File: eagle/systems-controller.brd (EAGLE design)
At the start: 80 x 40 mm, 52 parts, among them IC1 MK20DX256VLH7, IC2 MKL02Z32VFG4, IC3 TPS6214XRGT, J1 SIG, J2 PWR, J3 GND, Q1 FA-238, Q2 PMV20ENR, Q3 PMV20ENR, Q4 PMV20ENR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

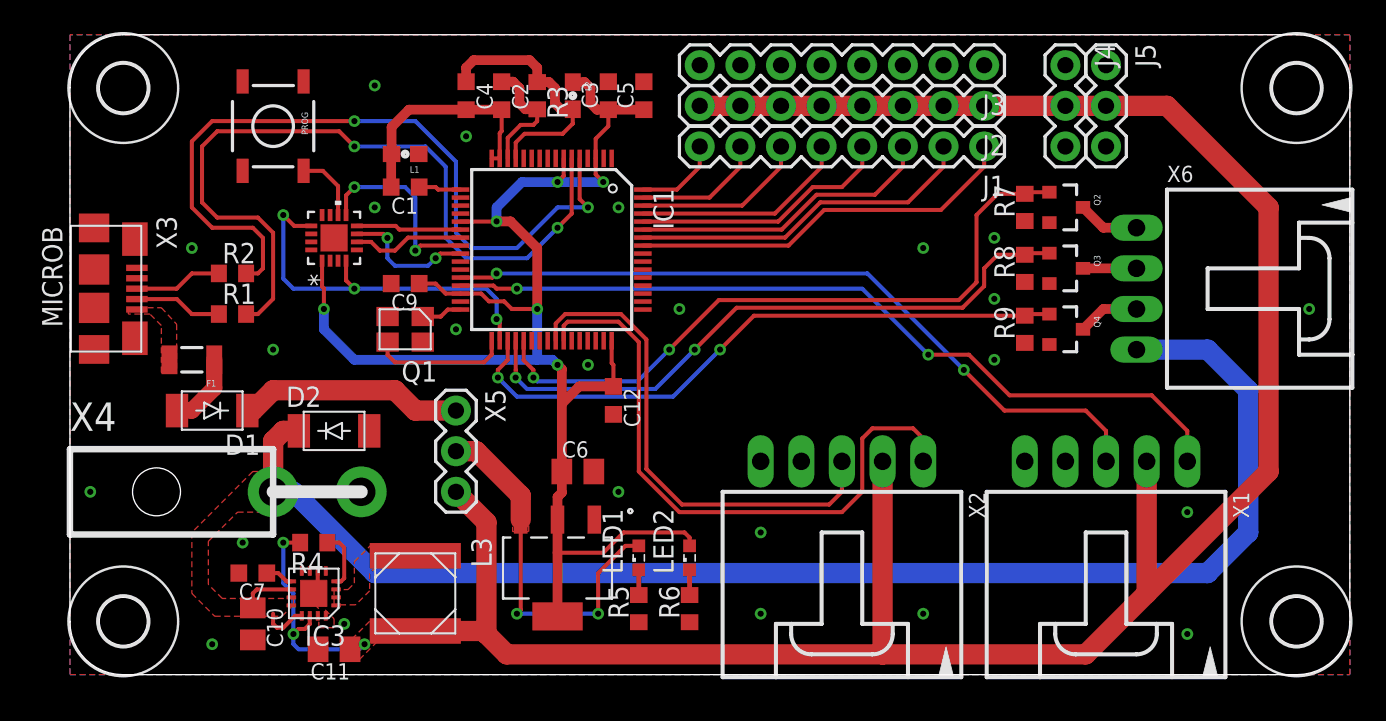
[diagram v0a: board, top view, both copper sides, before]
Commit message: added pwm headers
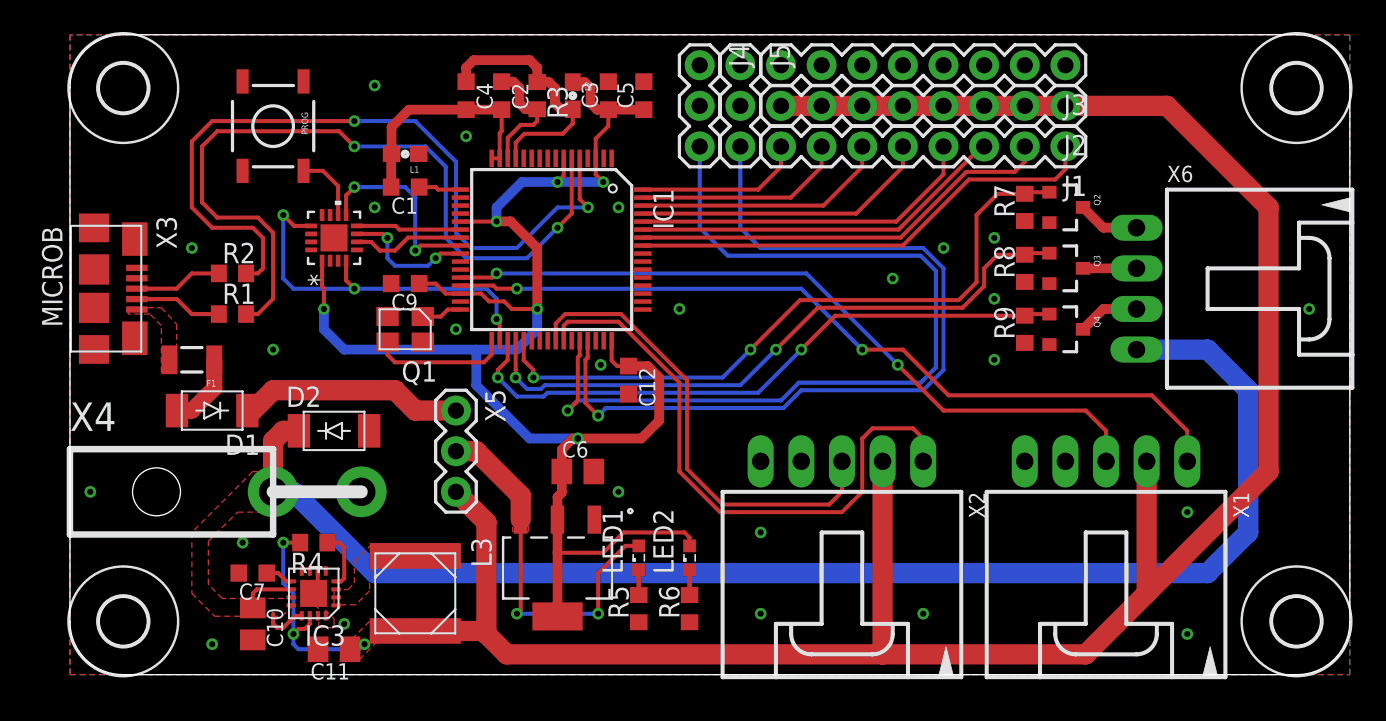
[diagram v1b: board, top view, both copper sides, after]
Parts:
- moved J4 22.9 mm to (39.4, 38.1)
- moved J5 22.9 mm to (41.9, 38.1)
- moved J1 5.08 mm to (62.2, 33.0)
- moved J2 5.08 mm to (62.2, 35.6)
- moved J3 5.08 mm to (62.2, 38.1)
- moved C12 1.59 mm to (34.9, 18.4)
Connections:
- net +5V: no longer J4.2, J5.2
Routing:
- net PWM1: track 0.00 -> 55.8 mm, vias 0 -> 1
- net PWM2: track 0.00 -> 53.0 mm, vias 0 -> 1
- net +3V3: track 92.9 -> 102.0 mm
- net CH4: track 16.4 -> 21.8 mm
- net CH1: track 24.6 -> 29.8 mm
- net +5V: track 157.5 -> 152.5 mm
- net CH7: track 8.16 -> 13.2 mm
- net CH8: track 5.42 -> 10.5 mm
- net CH5: track 13.7 -> 18.7 mm
- net CH6: track 10.9 -> 16.0 mm
- net CH2: track 21.9 -> 26.8 mm
- net CH3: track 19.2 -> 23.5 mm
- net ENC2B: track 39.0 -> 37.5 mm
- net ENC2A: track 31.1 -> 29.6 mm
- net GND: vias 24 -> 25

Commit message: made silkscreen pretty!
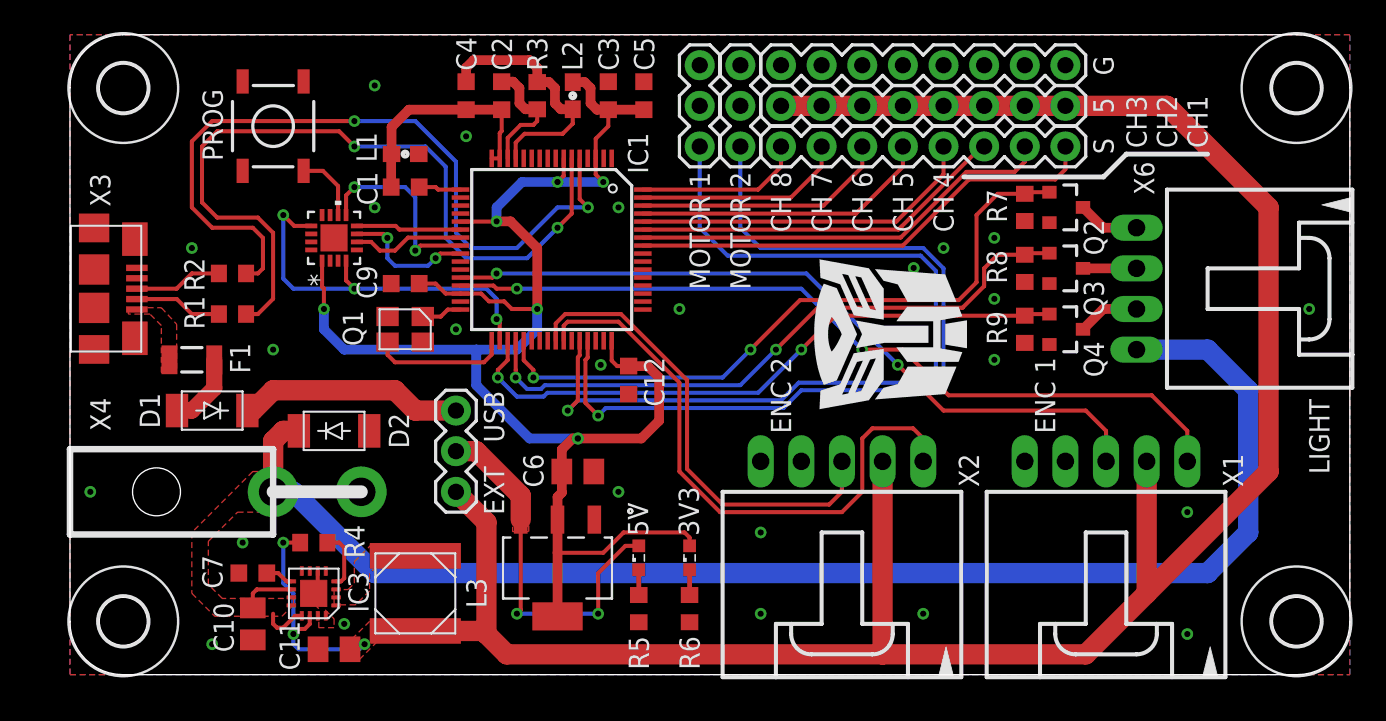
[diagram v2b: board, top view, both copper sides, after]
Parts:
- renumbered LED1 to 5V, LED2 to 3V3
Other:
- board text added: "5"
- board text added: "Autobot Systems Controller Blue Marble Security Enterprice Nathan Duprey 2016"
- board text added: "CH 4"
- board text added: "CH 5"
- board text added: "CH 6"
- board text added: "CH 7"
- board text added: "CH 8"
- board text added: "CH3 CH2 CH1"
- board text added: "ENC 1"
- board text added: "ENC 2"
- board text added: "EXT USB"
- board text added: "G"
- board text added: "LIGHT"
- board text added: "MOTOR 1"
- board text added: "MOTOR 2"
- board text added: "S"
